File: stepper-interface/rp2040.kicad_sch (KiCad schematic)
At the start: 31 parts, among them J1301 Connector_USB_C_Receptacle_10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, SW1301 Switch_Tactile_SPST-NO_SMT_Si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, U1301 Linear_3.3V_1A, U1302 MCU_RP2040, U1303 Memory_Flash_W25Q128JVZPIQ, Y1301 Crystal_12MHz

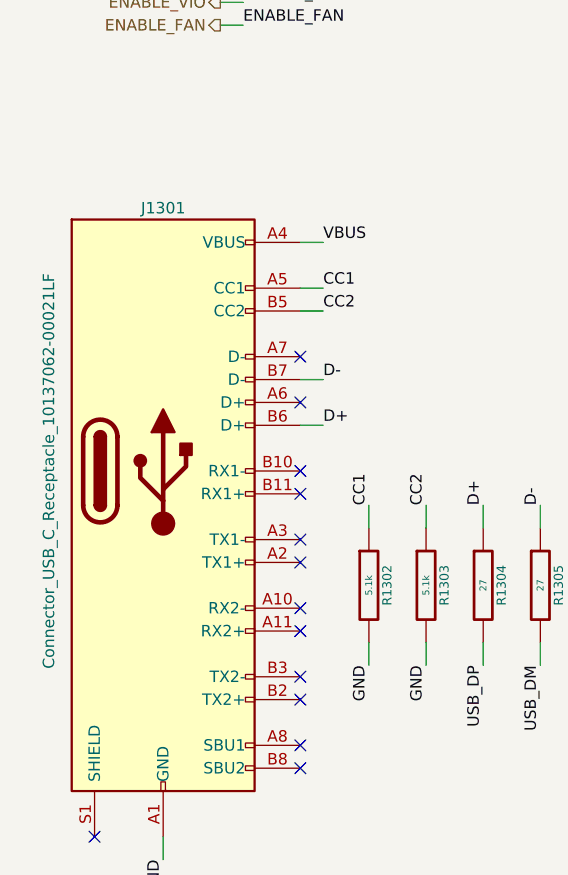
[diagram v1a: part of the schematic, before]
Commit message: Switch USB-C connector
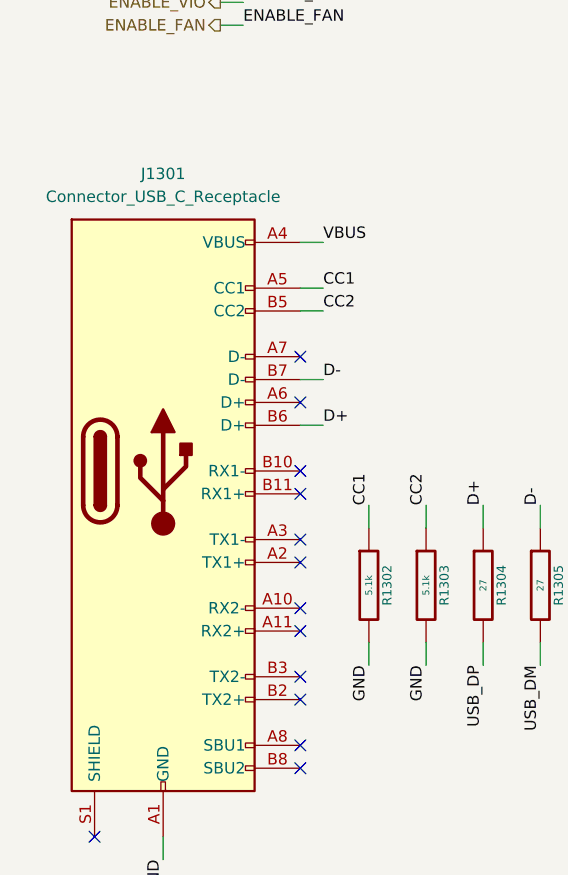
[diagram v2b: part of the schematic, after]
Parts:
- removed J1301: Connector_USB_C_Receptacle_10137062-00021LF, Janelia:USB_C_Receptacle_Amphenol_10137062-00021LF, symbol Janelia:Connector_USB_C_Receptacle_10137062-00021LF
- added J1301: Connector_USB_C_Receptacle, Janelia:USB_C_Receptacle_Amphenol_10152803-00011LF, symbol Janelia:Connector_USB_C_Receptacle_10152803-00011LF
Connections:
- net CC1: now also J1301.A5 (CC1)
- net CC2: now also J1301.B5 (CC2)
- net D+: now also J1301.B6 (D+)
- net D-: now also J1301.B7 (D-)
- net GND: now also J1301.A1 (GND), J1301.A12 (GND), J1301.B1 (GND), J1301.B12 (GND)
- net VBUS: now also J1301.A4 (VBUS), J1301.A9 (VBUS), J1301.B4 (VBUS), J1301.B9 (VBUS)
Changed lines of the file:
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@@
+    )
+  )
+  (symbol (lib_id "Janelia:Connector_USB_C_Receptacle_10152803-00011LF") (at 31.75 100.33 0) (unit 1)
+    (in_bom yes) (on_board yes) (dnp no) (fields_autoplaced)
+    (property "Reference" "J1301" (at 31.75 67.31 0)
+      (effects (font (size 1.27 1.27)))
+    )
+    (property "Value" "Connector_USB_C_Receptacle" (at 31.75 69.85 0)
+      (effects (font (size 1.27 1.27)))
+    )
+    (property "Footprint" "Janelia:USB_C_Receptacle_Amphenol_10152803-00011LF" (at 35.56 100.33 0)
+      (effects (font (size 1.27 1.27)) hide)
+    )
+    (property "Datasheet" "" (at 35.56 100.33 0)
+      (effects (font (size 1.27 1.27)) hide)
+    )
+    (property "Synopsis" "USB 3.2 TYPE C GEN 2 RECEPTACLE" (at 31.75 100.33 0)
+      (effects (font (size 1.27 1.27)) hide)
+    )
+    (property "Manufacturer" "Amphenol ICC (FCI)" (at 31.75 100.33 0)
+      (effects (font (size 1.27 1.27)) hide)
+    )
+    (property "Manufacturer Part Number" "10152803-00011LF" (at 31.75 100.33 0)
+      (effects (font (size 1.27 1.27)) hide)
+    )
+    (property "Vendor" "Digi-Key" (at 31.75 100.33 0)
+      (effects (font (size 1.27 1.27)) hide)
+    )
+    (property "Vendor Part Number" "609-10152803-00011LFCT-ND" (at 31.75 100.33 0)
+      (effects (font (size 1.27 1.27)) hide)
+    )
+    (pin "A6")
+    (pin "B11")
+    (pin "B3")
+    (pin "B8")
+    (pin "B6")
+    (pin "B9")
+    (pin "B2")
+    (pin "B4")
+    (pin "A8")
+    (pin "B10")
+    (pin "B5")
+    (pin "A12")
+    (pin "A7")
+    (pin "A11")
+    (pin "B1")
+    (pin "B7")
+    (pin "B12")
+    (pin "A3")
+    (pin "A2")
+    (pin "A10")
+    (pin "A4")
+    (pin "A1")
+    (pin "A5")
+    (pin "A9")
+    (pin "S1")
+    (instances
+      (project "stepper-interface"
+        (path "/df2b2e89-e055-4140-95de-f1df723db034/69dff8eb-dcc1-4f17-9e1d-cf8103035e92"
+          (reference "J1301") (unit 1)
+        )
+      )
     )
   )
@@
         )
       )
-    )
-  )
-  (symbol (lib_id "Janelia:Connector_USB_C_Receptacle_10137062-00021LF") (at 31.75 100.33 0) (unit 1)
-    (in_bom yes) (on_board yes) (dnp no)
-    (property "Reference" "J1301" (at 31.75 71.12 0)
-      (effects (font (size 1.27 1.27)))
-    )
-    (property "Value" "Connector_USB_C_Receptacle_10137062-00021LF" (at 19.05 100.33 90)
-      (effects (font (size 1.27 1.27)))
-    )
-    (property "Footprint" "Janelia:USB_C_Receptacle_Amphenol_10137062-00021LF" (at 35.56 100.33 0)
-      (effects (font (size 1.27 1.27)) hide)
-    )
-    (property "Datasheet" "https://www.usb.org/sites/default/files/documents/usb_type-c.zip" (at 35.56 100.33 0)
-      (effects (font (size 1.27 1.27)) hide)
-    )
-    (property "Synopsis" "CONN RCP USB3.1 TYPEC 24P SMD RA" (at 31.75 100.33 0)
-      (effects (font (size 1.27 1.27)) hide)
-    )
-    (property "Manufacturer" "Amphenol ICC (FCI)" (at 31.75 100.33 0)
-      (effects (font (size 1.27 1.27)) hide)
-    )
-    (property "Manufacturer Part Number" "10137062-00021LF" (at 31.75 100.33 0)
-      (effects (font (size 1.27 1.27)) hide)
-    )
-    (property "Vendor" "Digi-Key" (at 31.75 100.33 0)
-      (effects (font (size 1.27 1.27)) hide)
-    )
-    (property "Vendor Part Number" "609-6109-1-ND" (at 31.75 100.33 0)
-      (effects (font (size 1.27 1.27)) hide)
-    )
-    (pin "A5")
-    (pin "S1")
-    (pin "B2")
-    (pin "B3")
-    (pin "A1")
-    (pin "B10")
-    (pin "A9")
-    (pin "B4")
-    (pin "A7")
-    (pin "A8")
-    (pin "B8")
-    (pin "B9")
-    (pin "B6")
-    (pin "B7")
-    (pin "B12")
-    (pin "A6")
-    (pin "B11")
-    (pin "B5")
-    (pin "B1")
-    (pin "A4")
-    (pin "A3")
-    (pin "A2")
-    (pin "A12")
-    (pin "A11")
-    (pin "A10")
-    (instances
-      (project "stepper-interface"
-        (path "/df2b2e89-e055-4140-95de-f1df723db034/69dff8eb-dcc1-4f17-9e1d-cf8103035e92"
-          (reference "J1301") (unit 1)
-        )
-      )

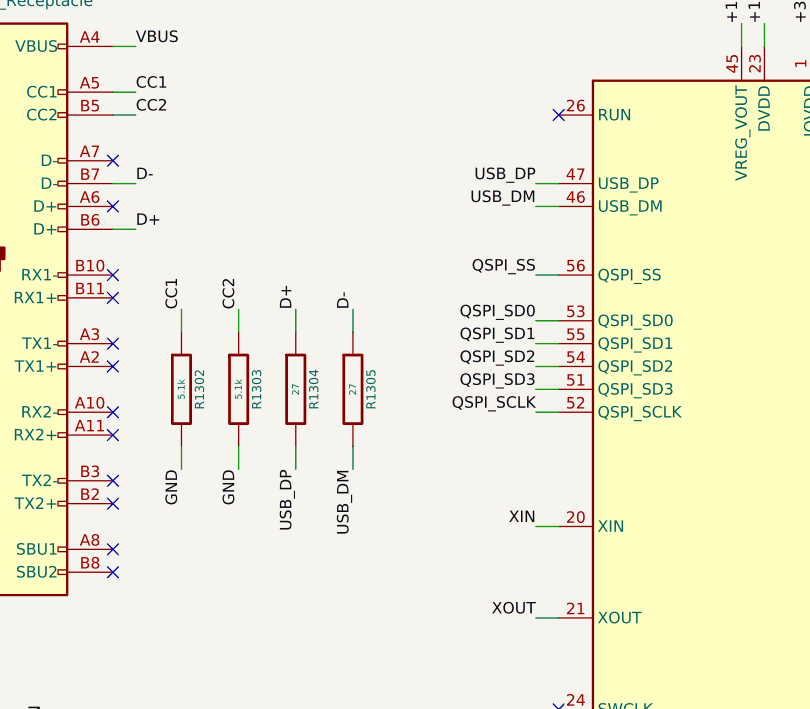
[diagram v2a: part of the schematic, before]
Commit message: Fix warnings on import from schematic to pcb
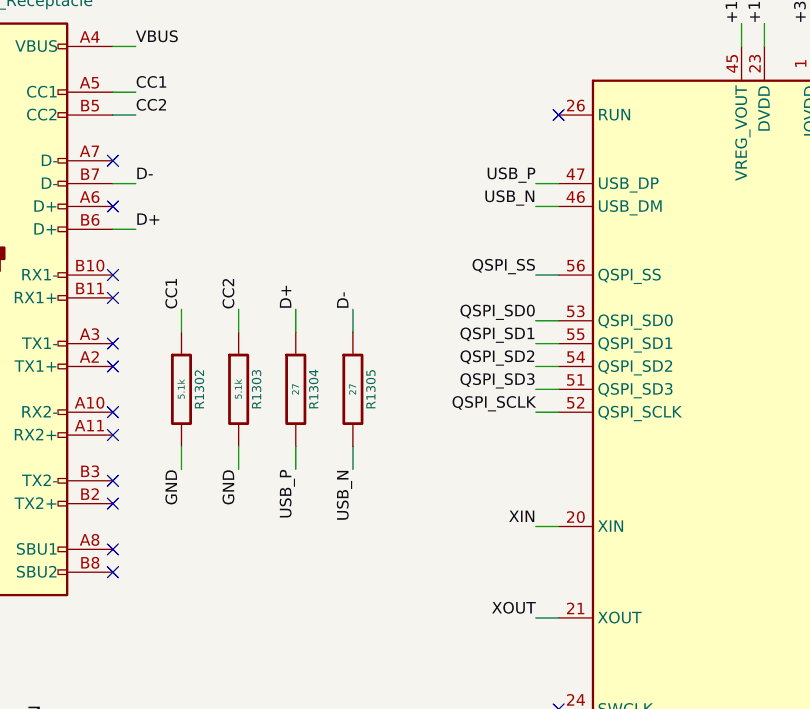
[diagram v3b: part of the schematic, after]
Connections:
- net at J1301.S1 (SHIELD): now also J1301.S2 (SHIELD), J1301.S3 (SHIELD), J1301.S4 (SHIELD)
- net USB_DM renamed USB_N
- net USB_DP renamed USB_P
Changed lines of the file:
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@@
   (title_block
     (title "stepper-interface")
-    (date "2024-04-30")
+    (date "2024-05-01")
     (rev "1.0")
     (company "Howard Hughes Medical Institute")
@@
     (effects (font (size 1.27 1.27)) (justify left bottom))
   )
-  (label "USB_DP" (at 93.98 90.17 180) (fields_autoplaced)
+  (label "USB_P" (at 93.98 90.17 180) (fields_autoplaced)
     (effects (font (size 1.27 1.27)) (justify right bottom))
   )
@@
     (effects (font (size 1.27 1.27)) (justify left bottom))
   )
-  (label "USB_DP" (at 67.31 121.92 270) (fields_autoplaced)
+  (label "USB_P" (at 67.31 121.92 270) (fields_autoplaced)
     (effects (font (size 1.27 1.27)) (justify right bottom))
   )
@@
     (effects (font (size 1.27 1.27)) (justify left bottom))
   )
-  (label "USB_DM" (at 73.66 121.92 270) (fields_autoplaced)
+  (label "USB_N" (at 73.66 121.92 270) (fields_autoplaced)
     (effects (font (size 1.27 1.27)) (justify right bottom))
   )
@@
     (effects (font (size 1.27 1.27)) (justify left bottom))
   )
-  (label "USB_DM" (at 93.98 92.71 180) (fields_autoplaced)
+  (label "USB_N" (at 93.98 92.71 180) (fields_autoplaced)
     (effects (font (size 1.27 1.27)) (justify right bottom))
   )
@@
     (pin "A9")
     (pin "S1")
+    (pin "S2")
+    (pin "S3")
+    (pin "S4")
     (instances
       (project "stepper-interface"
@@
     (pin "5")
     (pin "4")
-    (instances
-      (project "stepper-interface"
+    (pin "6")
+    (pin "7")
+    (pin "2")
+    (instances
+      (project "stepper-interface"

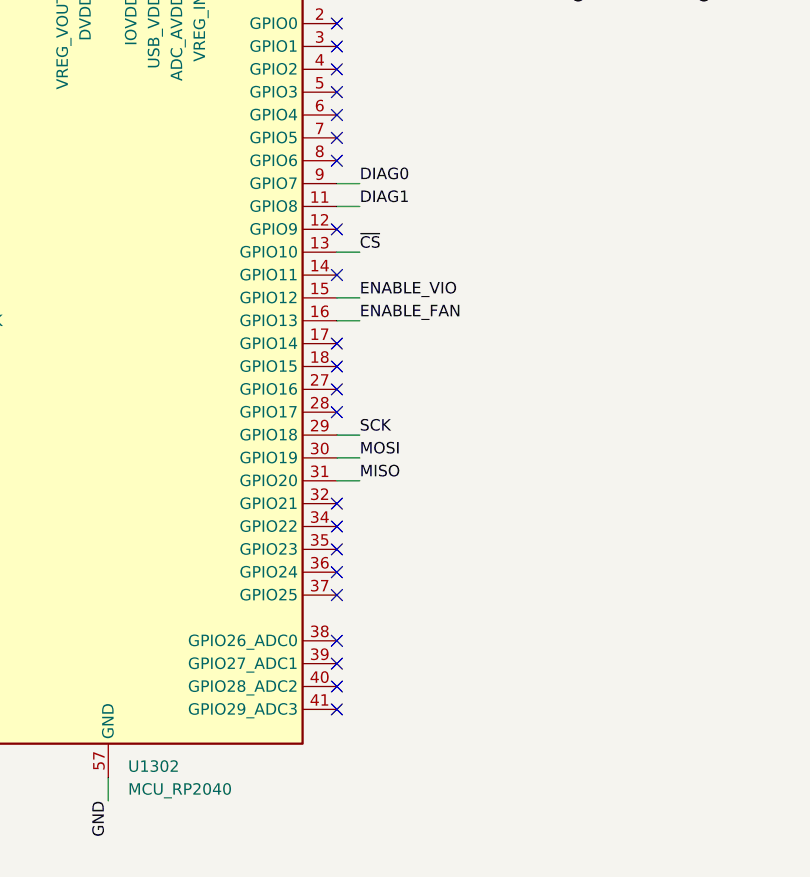
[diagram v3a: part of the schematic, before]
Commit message: Route more tracks
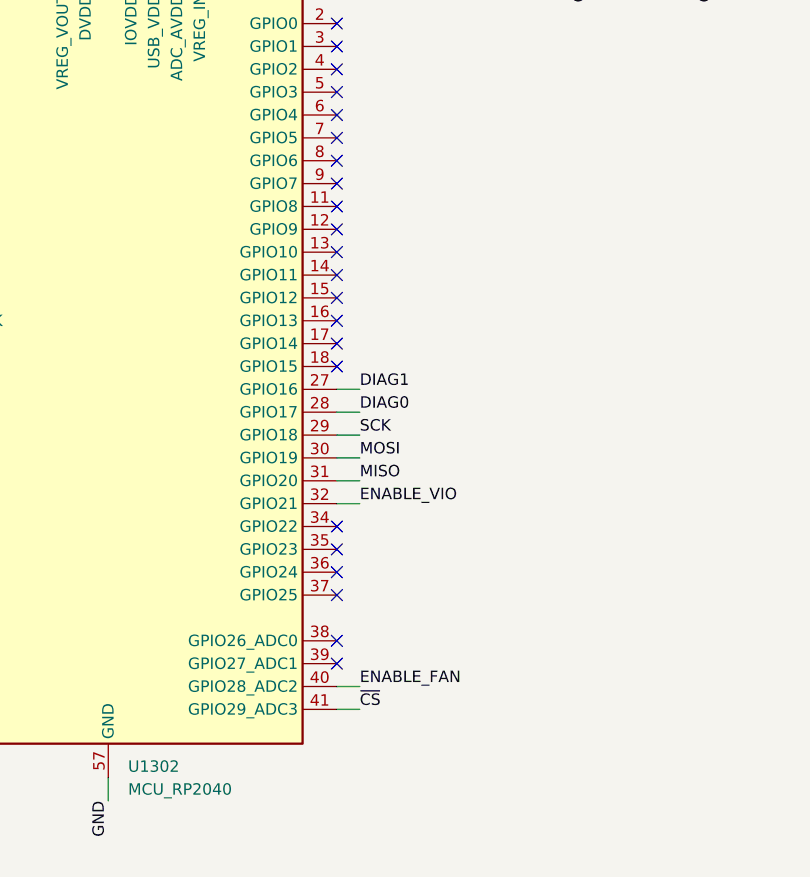
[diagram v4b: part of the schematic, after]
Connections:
- net DIAG0: now also U1302.28 (GPIO17); no longer U1302.9 (GPIO7)
- net DIAG1: now also U1302.27 (GPIO16); no longer U1302.11 (GPIO8)
- net ENABLE_FAN: now also U1302.40 (GPIO28_ADC2); no longer U1302.16 (GPIO13)
- net ENABLE_VIO: now also U1302.32 (GPIO21); no longer U1302.15 (GPIO12)
- net ~{CS}: now also U1302.41 (GPIO29_ADC3); no longer U1302.13 (GPIO10)
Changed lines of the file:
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@@
   (title_block
     (title "stepper-interface")
-    (date "2024-05-01")
+    (date "2024-05-02")
     (rev "1.0")
     (company "Howard Hughes Medical Institute")
@@
   (no_connect (at 147.32 120.65))
   (no_connect (at 46.99 102.87))
+  (no_connect (at 147.32 107.95))
   (no_connect (at 147.32 146.05))
-  (no_connect (at 147.32 158.75))
   (no_connect (at 46.99 87.63))
   (no_connect (at 46.99 133.35))
@@
   (no_connect (at 46.99 123.19))
   (no_connect (at 147.32 90.17))
-  (no_connect (at 147.32 135.89))
+  (no_connect (at 147.32 102.87))
   (no_connect (at 147.32 92.71))
   (no_connect (at 147.32 143.51))
   (no_connect (at 129.54 39.37))
   (no_connect (at 147.32 95.25))
-  (no_connect (at 147.32 125.73))
+  (no_connect (at 147.32 113.03))
   (no_connect (at 147.32 151.13))
   (no_connect (at 46.99 118.11))
-  (no_connect (at 147.32 156.21))
+  (no_connect (at 147.32 115.57))
   (no_connect (at 147.32 118.11))
   (no_connect (at 147.32 97.79))
@@
   (no_connect (at 147.32 105.41))
   (no_connect (at 147.32 110.49))
-  (no_connect (at 147.32 123.19))
+  (no_connect (at 147.32 100.33))
   (wire (pts (xy 223.52 134.62) (xy 220.98 134.62))
     (stroke (width 0) (type default))
@@
     (stroke (width 0) (type default))
   )
-  (wire (pts (xy 147.32 113.03) (xy 149.86 113.03))
+  (wire (pts (xy 147.32 135.89) (xy 149.86 135.89))
     (stroke (width 0) (type default))
   )
@@
     (stroke (width 0) (type default))
   )
-  (wire (pts (xy 147.32 115.57) (xy 149.86 115.57))
+  (wire (pts (xy 147.32 156.21) (xy 149.86 156.21))
     (stroke (width 0) (type default))
   )
@@
     (stroke (width 0) (type default))
   )
-  (wire (pts (xy 147.32 107.95) (xy 149.86 107.95))
+  (wire (pts (xy 147.32 158.75) (xy 149.86 158.75))
     (stroke (width 0) (type default))
   )
@@
     (stroke (width 0) (type default))
   )
-  (wire (pts (xy 147.32 100.33) (xy 149.86 100.33))
+  (wire (pts (xy 147.32 125.73) (xy 149.86 125.73))
     (stroke (width 0) (type default))
   )
@@
     (stroke (width 0) (type default))
   )
-  (wire (pts (xy 147.32 102.87) (xy 149.86 102.87))
+  (wire (pts (xy 147.32 123.19) (xy 149.86 123.19))
     (stroke (width 0) (type default))
   )
@@
     (stroke (width 0) (type default))
   )
-  (label "ENABLE_VIO" (at 149.86 113.03 0) (fields_autoplaced)
+  (label "ENABLE_VIO" (at 149.86 135.89 0) (fields_autoplaced)
     (effects (font (size 1.27 1.27)) (justify left bottom))
   )
@@
     (effects (font (size 1.27 1.27)) (justify left bottom))
   )
-  (label "~{CS}" (at 149.86 107.95 0) (fields_autoplaced)
+  (label "~{CS}" (at 149.86 158.75 0) (fields_autoplaced)
     (effects (font (size 1.27 1.27)) (justify left bottom))
   )
@@
     (effects (font (size 1.27 1.27)) (justify left bottom))
   )
-  (label "DIAG0" (at 149.86 100.33 0) (fields_autoplaced)
+  (label "DIAG0" (at 149.86 125.73 0) (fields_autoplaced)
     (effects (font (size 1.27 1.27)) (justify left bottom))
   )
@@
     (effects (font (size 1.27 1.27)) (justify right bottom))
   )
-  (label "ENABLE_FAN" (at 149.86 115.57 0) (fields_autoplaced)
+  (label "ENABLE_FAN" (at 149.86 156.21 0) (fields_autoplaced)
     (effects (font (size 1.27 1.27)) (justify left bottom))
   )
@@
     (effects (font (size 1.27 1.27)) (justify right bottom))
   )
-  (label "DIAG1" (at 149.86 102.87 0) (fields_autoplaced)
-    (effects (font (size 1.27 1.27)) (justify left bottom))
-  )
+  (label "DIAG1" (at 149.86 123.19 0) (fields_autoplaced)
+    (effects (font (size 1.27 1.27)) (justify left bottom))
+  )

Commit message: Finish routing
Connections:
- net VBUS: no longer J1301.A9 (VBUS), J1301.B4 (VBUS)
- now unconnected: J1301.S1 (SHIELD), J1301.S2 (SHIELD), J1301.S3 (SHIELD), J1301.S4 (SHIELD)
- no-connect marks 39 -> 44
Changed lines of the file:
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@@
   (title_block
     (title "stepper-interface")
-    (date "2024-05-02")
+    (date "2024-05-03")
     (rev "1.0")
     (company "Howard Hughes Medical Institute")
@@
   (no_connect (at 46.99 102.87))
   (no_connect (at 147.32 107.95))
+  (no_connect (at 16.51 127))
   (no_connect (at 147.32 146.05))
   (no_connect (at 46.99 87.63))
@@
   (no_connect (at 147.32 102.87))
   (no_connect (at 147.32 92.71))
+  (no_connect (at 31.75 67.31))
   (no_connect (at 147.32 143.51))
   (no_connect (at 129.54 39.37))
@@
   (no_connect (at 46.99 118.11))
   (no_connect (at 147.32 115.57))
+  (no_connect (at 16.51 124.46))
   (no_connect (at 147.32 118.11))
   (no_connect (at 147.32 97.79))
@@
   (no_connect (at 96.52 148.59))
   (no_connect (at 147.32 138.43))
-  (no_connect (at 24.13 140.97))
+  (no_connect (at 16.51 121.92))
   (no_connect (at 147.32 153.67))
   (no_connect (at 46.99 115.57))
+  (no_connect (at 16.51 129.54))
   (no_connect (at 147.32 105.41))
+  (no_connect (at 29.21 67.31))
   (no_connect (at 147.32 110.49))
   (no_connect (at 147.32 100.33))
@@
     (stroke (width 0) (type default))
   )
+  (wire (pts (xy 34.29 140.97) (xy 34.29 143.51))
+    (stroke (width 0) (type default))
+  )
   (wire (pts (xy 119.38 74.93) (xy 119.38 72.39))
     (stroke (width 0) (type default))
@@
     (stroke (width 0) (type default))
   )
+  (wire (pts (xy 29.21 140.97) (xy 29.21 143.51))
+    (stroke (width 0) (type default))
+  )
   (wire (pts (xy 127 74.93) (xy 127 72.39))
     (stroke (width 0) (type default))
@@
     (stroke (width 0) (type default))
   )
+  (wire (pts (xy 26.67 67.31) (xy 26.67 64.77))
+    (stroke (width 0) (type default))
+  )
   (wire (pts (xy 250.19 111.76) (xy 247.65 111.76))
     (stroke (width 0) (type default))
@@
     (stroke (width 0) (type default))
   )
-  (wire (pts (xy 46.99 74.93) (xy 49.53 74.93))
+  (wire (pts (xy 34.29 67.31) (xy 34.29 64.77))
     (stroke (width 0) (type default))
   )
@@
     (stroke (width 0) (type default))
   )
+  (wire (pts (xy 26.67 140.97) (xy 26.67 143.51))
+    (stroke (width 0) (type default))
+  )
   (wire (pts (xy 60.96 106.68) (xy 60.96 104.14))
     (stroke (width 0) (type default))
@@
     (effects (font (size 1.27 1.27)) (justify right bottom))
   )
+  (label "GND" (at 34.29 143.51 270) (fields_autoplaced)
+    (effects (font (size 1.27 1.27)) (justify right bottom))
+  )
   (label "GND" (at 203.2 76.2 270) (fields_autoplaced)
     (effects (font (size 1.27 1.27)) (justify right bottom))
@@
     (effects (font (size 1.27 1.27)) (justify right bottom))
   )
+  (label "GND" (at 29.21 143.51 270) (fields_autoplaced)
+    (effects (font (size 1.27 1.27)) (justify right bottom))
+  )
   (label "ENABLE_FAN" (at 40.64 50.8 0) (fields_autoplaced)
     (effects (font (size 1.27 1.27)) (justify left bottom))
@@
     (effects (font (size 1.27 1.27)) (justify left bottom))
   )
+  (label "VBUS" (at 26.67 64.77 90) (fields_autoplaced)
+    (effects (font (size 1.27 1.27)) (justify left bottom))
+  )
   (label "QSPI_SD0" (at 220.98 139.7 180) (fields_autoplaced)
     (effects (font (size 1.27 1.27)) (justify right bottom))
@@
     (effects (font (size 1.27 1.27)) (justify left bottom))
   )
-  (label "VBUS" (at 49.53 74.93 0) (fields_autoplaced)
+  (label "VBUS" (at 34.29 64.77 90) (fields_autoplaced)
     (effects (font (size 1.27 1.27)) (justify left bottom))
   )
   (label "GND" (at 31.75 143.51 270) (fields_autoplaced)
+    (effects (font (size 1.27 1.27)) (justify right bottom))
+  )
+  (label "GND" (at 26.67 143.51 270) (fields_autoplaced)
     (effects (font (size 1.27 1.27)) (justify right bottom))
   )
@@
   )
   (symbol (lib_id "Janelia:Connector_USB_C_Receptacle_10152803-00011LF") (at 31.75 100.33 0) (unit 1)
-    (in_bom yes) (on_board yes) (dnp no) (fields_autoplaced)
-    (property "Reference" "J1301" (at 31.75 67.31 0)
+    (in_bom yes) (on_board yes) (dnp no)
+    (property "Reference" "J1301" (at 41.91 71.12 0) (do_not_autoplace)
       (effects (font (size 1.27 1.27)))
     )
-    (property "Value" "Connector_USB_C_Receptacle" (at 31.75 69.85 0)
+    (property "Value" "Connector_USB_C_Receptacle" (at 20.32 100.33 90)
       (effects (font (size 1.27 1.27)))
     )
